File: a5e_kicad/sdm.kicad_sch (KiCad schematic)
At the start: 21 parts, among them U2 MX25U25645G, U7 A5EB013B-B23B

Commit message: Add LCSC part numbers and fix C102 footprint
Add a hidden LCSC field to 290 symbols from the JLCPCB parts match
(2026-10-23). Left without LCSC: U7, U15, L1 (not in the JLCPCB
library), C1/C2/C4 and L2-L5 (no value specified), J3 (no confident
match) and Y3 (the 12 pF Basic crystal does not suit the 27 pF load
caps). U2, U12, Y2 and J9 carry the exact-MPN LCSC numbers although
they currently show zero JLCPCB stock.

C102 (22U 6V3) had a 0201 footprint; no 22 uF 0201 part exists. Change
it to 0402 (C415703) like C5-C7.
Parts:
- D1, D2: LCSC (none) -> C3030991
- R10, R11, R12, R14, R15, R19, R20, R21, R8, R9: LCSC (none) -> C25744
- R16, R17: LCSC (none) -> C25130
- R18: LCSC (none) -> C4109
- R22: LCSC (none) -> C11702
- R4, R45, R7: LCSC (none) -> C25900
- U2: LCSC (none) -> C2802880
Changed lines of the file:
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@@
 			)
 		)
+		(property "LCSC" "C25744"
+			(at 80.772 93.98 90)
+			(hide yes)
+			(show_name no)
+			(do_not_autoplace no)
+			(effects
+				(font
+					(size 1.27 1.27)
+				)
+			)
+		)
 		(property "Datasheet" ""
 			(at 82.55 93.98 0)
@@
 			)
 		)
+		(property "LCSC" "C25744"
+			(at 219.202 26.67 90)
+			(hide yes)
+			(show_name no)
+			(do_not_autoplace no)
+			(effects
+				(font
+					(size 1.27 1.27)
+				)
+			)
+		)
 		(property "Datasheet" ""
 			(at 220.98 26.67 0)
@@
 			)
 		)
+		(property "LCSC" "C25744"
+			(at 70.612 93.98 90)
+			(hide yes)
+			(show_name no)
+			(do_not_autoplace no)
+			(effects
+				(font
+					(size 1.27 1.27)
+				)
+			)
+		)
 		(property "Datasheet" ""
 			(at 72.39 93.98 0)
@@
 			)
 		)
+		(property "LCSC" "C11702"
+			(at 229.362 26.67 90)
+			(hide yes)
+			(show_name no)
+			(do_not_autoplace no)
+			(effects
+				(font
+					(size 1.27 1.27)
+				)
+			)
+		)
 		(property "Datasheet" ""
 			(at 231.14 26.67 0)
@@
 			)
 		)
+		(property "LCSC" "C25744"
+			(at 75.692 93.98 90)
+			(hide yes)
+			(show_name no)
+			(do_not_autoplace no)
+			(effects
+				(font
+					(size 1.27 1.27)
+				)
+			)
+		)
 		(property "Datasheet" ""
 			(at 77.47 93.98 0)
@@
 			)
 		)
+		(property "LCSC" "C3030991"
+			(at 100.33 162.56 0)
+			(hide yes)
+			(show_name no)
+			(do_not_autoplace no)
+			(effects
+				(font
+					(size 1.27 1.27)
+				)
+			)
+		)
 		(property "Datasheet" "https://www.we-online.com/components/products/datasheet/150060RS75000.pdf"
 			(at 100.33 162.56 0)
@@
 			)
 		)
+		(property "LCSC" "C25744"
+			(at 87.122 46.99 90)
+			(hide yes)
+			(show_name no)
+			(do_not_autoplace no)
+			(effects
+				(font
+					(size 1.27 1.27)
+				)
+			)
+		)
 		(property "Datasheet" ""
 			(at 88.9 46.99 0)
@@
 			)
 		)
+		(property "LCSC" "C4109"
+			(at 188.722 123.19 90)
+			(hide yes)
+			(show_name no)
+			(do_not_autoplace no)
+			(effects
+				(font
+					(size 1.27 1.27)
+				)
+			)
+		)
 		(property "Datasheet" ""
 			(at 190.5 123.19 0)
@@
 			)
 		)
+		(property "LCSC" "C25744"
+			(at 214.122 26.67 90)
+			(hide yes)
+			(show_name no)
+			(do_not_autoplace no)
+			(effects
+				(font
+					(size 1.27 1.27)
+				)
+			)
+		)
 		(property "Datasheet" ""
 			(at 215.9 26.67 0)
@@
 			)
 		)
+		(property "LCSC" "C25130"
+			(at 110.49 164.338 90)
+			(hide yes)
+			(show_name no)
+			(do_not_autoplace no)
+			(effects
+				(font
+					(size 1.27 1.27)
+				)
+			)
+		)
 		(property "Datasheet" ""
 			(at 110.49 162.56 0)
@@
 			)
 		)
+		(property "LCSC" "C25744"
+			(at 82.042 46.99 90)
+			(hide yes)
+			(show_name no)
+			(do_not_autoplace no)
+			(effects
+				(font
+					(size 1.27 1.27)
+				)
+			)
+		)
 		(property "Datasheet" ""
 			(at 83.82 46.99 0)
@@
 			)
 		)
+		(property "LCSC" "C25900"
+			(at 60.452 93.98 90)
+			(hide yes)
+			(show_name no)
+			(do_not_autoplace no)
+			(effects
+				(font
+					(size 1.27 1.27)
+				)
+			)
+		)
 		(property "Datasheet" ""
 			(at 62.23 93.98 0)
@@
 			)
 		)
+		(property "LCSC" "C25130"
+			(at 110.49 182.118 90)
+			(hide yes)
+			(show_name no)
+			(do_not_autoplace no)
+			(effects
+				(font
+					(size 1.27 1.27)
+				)
+			)
+		)
 		(property "Datasheet" ""
 			(at 110.49 180.34 0)
@@
 			)
 		)
+		(property "LCSC" "C25900"
+			(at 55.372 133.35 90)
+			(hide yes)
+			(show_name no)
+			(do_not_autoplace no)
+			(effects
+				(font
+					(size 1.27 1.27)
+				)
+			)
+		)
 		(property "Datasheet" ""
 			(at 57.15 133.35 0)
@@
 			)
 		)
+		(property "LCSC" "C25900"
+			(at 50.292 133.35 90)
+			(hide yes)
+			(show_name no)
+			(do_not_autoplace no)
+			(effects
+				(font
+					(size 1.27 1.27)
+				)
+			)
+		)
 		(property "Datasheet" ""
 			(at 52.07 133.35 0)
@@
 			)
 		)
+		(property "LCSC" "C3030991"
+			(at 100.33 180.34 0)
+			(hide yes)
+			(show_name no)
+			(do_not_autoplace no)
+			(effects
+				(font
+					(size 1.27 1.27)
+				)
+			)
+		)
 		(property "Datasheet" "https://www.we-online.com/components/products/datasheet/150060RS75000.pdf"
 			(at 100.33 180.34 0)
@@
 			)
 		)
+		(property "LCSC" "C25744"
+			(at 224.282 26.67 90)
+			(hide yes)
+			(show_name no)
+			(do_not_autoplace no)
+			(effects
+				(font
+					(size 1.27 1.27)
+				)
+			)
+		)
 		(property "Datasheet" ""
 			(at 226.06 26.67 0)
@@
 			)
 		)
+		(property "LCSC" "C25744"
+			(at 92.202 46.99 90)
+			(hide yes)
+			(show_name no)
+			(do_not_autoplace no)
+			(effects
+				(font
+					(size 1.27 1.27)
+				)
+			)
+		)
 		(property "Datasheet" ""
 			(at 93.98 46.99 0)
@@
 			)
 		)
+		(property "LCSC" "C25744"
+			(at 65.532 93.98 90)
+			(hide yes)
+			(show_name no)
+			(do_not_autoplace no)
+			(effects
+				(font
+					(size 1.27 1.27)
+				)
+			)
+		)
 		(property "Datasheet" ""
 			(at 67.31 93.98 0)
@@
 			(at 46.99 55.88 0)
 			(hide yes)
+			(show_name no)
+			(do_not_autoplace no)
+			(effects
+				(font
+					(size 1.27 1.27)
+				)
+			)
+		)
+		(property "LCSC" "C2802880"
+			(at 46.99 55.88 0)
+			(hide yes)

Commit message: U12 -> H9HCNNN8KUMLHR-NME, U2 -> IS25WP128-RHLE (values, LCSC, datasheets)
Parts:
- U2: value MX25U25645G -> IS25WP128-RHLE; LCSC C2802880 -> C1349419
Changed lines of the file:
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@@
 			)
 		)
-		(property "Value" "MX25U25645G"
+		(property "Value" "IS25WP128-RHLE"
 			(at 46.99 70.88 0)
 			(show_name no)
@@
 			)
 		)
-		(property "LCSC" "C2802880"
+		(property "LCSC" "C1349419"
 			(at 46.99 55.88 0)
 			(hide yes)
@@
 			)
 		)
-		(property "Datasheet" "https://www.macronix.com/Lists/Datasheet/Attachments/8738/MX25U25645G,%201.8V,%20256Mb,%20v1.4.pdf"
+		(property "Datasheet" "https://www.lcsc.com/datasheet/C1349419.pdf"
 			(at 46.99 55.88 0)
 			(hide yes)
@@
 			)
 		)
-		(property "Description" "256Mb 1.8V QSPI NOR Flash, 24-ball CSP/BGA (5x5, A1 depopulated), SFDP + 1-1-1/1-4-4/4-4-4, dedicated RESET# - Agilex 5 SDM ASx4 boot compatible"
+		(property "Description" "128Mb 1.8V QSPI NOR flash, dedicated RESET# (A4), SFDP, 24-ball TFBGA 6x8 mm 5x5 array - Agilex 5 SDM ASx4 boot compatible"
 			(at 46.99 55.88 0)
 			(hide yes)

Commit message: Power/config review against the Altera docs: bank 6A, MSEL, resets, fabric clock
Checked against Pin Connection Guidelines 813266, Power Management UG
813161, Configuration UG 813773 and the data sheet 813918; findings are
in AGILEX_POWER_CONFIG_CHECKLIST.md.

- VCCIO_HVIO_6A moves from the VCCPT 1V8 regulator to 3V3. PCG table 32
  requires a dedicated VCCIO_HVIO supply. CE19 no longer takes the 1.8 V
  sdm_clk25.
- Y4 (YXC OT3225100MJBA4SL, 100 MHz 3.3 V CMOS, C4353707) drives the
  dangling clk100 net to AE11 (bank 6G PLLREFCLK1), giving the fabric a
  PLL reference that doesn't depend on the HPS. The clock sheet pin
  clk2_N is renamed clk100.
- MSEL 001 (AS fast) -> 011 (AS normal): fast mode needs all supplies
  ramped within 10 ms, which the sequenced regulators don't guarantee.
  R45 now goes to 1V8, and R4 gets its own GND.
- R264 10k pull-up on HPS_COLD_nRESET (SDM_IO10), as the PCG requires.
- R9/R10 (INIT_DONE/CONF_DONE pull-ups) DNP; the internal pull-downs
  hold the pins low until configuration.
- Note on the fpga_power sheet and the PCB (Cmts.User): ferrite + cap
  isolation filters on the PLL/ADC rails are recommended but not
  fitted yet.
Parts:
- added R264: 10K, Resistor_SMD:R_0402_1005Metric, symbol Device:R
- R10, R9: now not fitted
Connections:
- net 1V8: now also R45.2, R264.1
- net GND: no longer R45.2
- net ~{hpscold_rstn}: now also R264.2
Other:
- note added: "R264: HPS_COLD_nRESET pull-up, 1-10k to VCCIO_SDM (PCG 813266). MSEL = 011 (AS normal): R45 to 1V8. R9/R10 DNP: SDM_IO0/IO16 have internal pull-downs."
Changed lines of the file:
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@@
 	)
 	(junction
-		(at 57.15 139.7)
-		(diameter 0)
-		(color 0 0 0 0)
-	)
-	(junction
 		(at 74.93 87.63)
 		(diameter 0)
@@
 	(wire
 		(pts
-			(xy 57.15 139.7) (xy 52.07 139.7)
-		)
-		(stroke
-			(width 0)
-			(type default)
-		)
-	)
-	(wire
-		(pts
 			(xy 95.25 162.56) (xy 96.52 162.56)
 		)
@@
 		(on_board yes)
 		(in_pos_files yes)
-		(dnp no)
+		(dnp yes)
 		(property "Reference" "R9"
 			(at 72.39 90.17 0)
@@
 		(on_board yes)
 		(in_pos_files yes)
-		(dnp no)
+		(dnp yes)
 		(property "Reference" "R10"
 			(at 77.47 90.17 0)
@@
 	)
 	(symbol
-		(lib_id "power:GND")
-		(at 57.15 139.7 0)
+		(lib_id "power:+3V3")
+		(at 57.15 139.7 180)
 		(unit 1)
 		(body_style 1)
@@
 		(fields_autoplaced yes)
 		(property "Reference" "#PWR021"
-			(at 57.15 146.05 0)
+			(at 57.15 143.51 0)
 			(hide yes)
 			(show_name no)
@@
 			)
 		)
-		(property "Value" "GND"
-			(at 57.15 144.78 0)
+		(property "Value" "1V8"
+			(at 57.15 134.62 0)
 			(show_name no)
 			(do_not_autoplace no)
@@
 			)
 		)
-		(property "Description" "Power symbol creates a global label with name \"GND\" , ground"
+		(property "Description" "Power symbol creates a global label with name \"+3V3\""
 			(at 57.15 139.7 0)
 			(hide yes)
@@
 		)
 		(instances
-			(project "DBM_A5E013"
-				(path "/267d02d2-570f-41a1-8015-b378cedbc665/8aaf6c2b-ae6e-4499-806d-67948f95803c"
-					(reference "#PWR0202")
-					(unit 1)
-				)
-			)
 			(project "agilex_3_soc"
 				(path "/a5b98d95-6877-4284-904f-d04e32723ae0/8aaf6c2b-ae6e-4499-806d-67948f95803c"
@@
 		)
 	)
-)
+	(wire
+		(pts
+			(xy 82.55 87.63) (xy 87.63 87.63)
+		)
+		(stroke
+			(width 0)
+			(type default)
+		)
+	)
+	(junction
+		(at 82.55 87.63)
+		(diameter 0)
+		(color 0 0 0 0)
+	)
+	(wire
+		(pts
+			(xy 87.63 87.63) (xy 87.63 90.17)
+		)
+		(stroke
+			(width 0)
+			(type default)
+		)
+	)
+	(symbol
+		(lib_id "Device:R")
+		(at 87.63 93.98 0)
+		(unit 1)
+		(body_style 1)
+		(exclude_from_sim no)
+		(in_bom yes)
+		(on_board yes)
+		(in_pos_files yes)
+		(dnp no)
+		(property "Reference" "R264"
+			(at 87.63 90.17 0)
+			(show_name no)
+			(do_not_autoplace no)
+			(effects
+				(font
+					(size 1.27 1.27)
+				)
+				(justify left)
+			)
+		)
+		(property "Value" "10K"
+			(at 87.63 97.79 0)
+			(show_name no)
+			(do_not_autoplace no)
+			(effects
+				(font
+					(size 1.27 1.27)
+				)
+				(justify left)
+			)
+		)
+		(property "Footprint" "Resistor_SMD:R_0402_1005Metric"
+			(at 85.852 93.98 90)
+			(hide yes)
+			(show_name no)
+			(do_not_autoplace no)
+			(effects
+				(font
+					(size 1.27 1.27)
+				)
+			)
+		)
+		(property "LCSC" "C25744"
+			(at 85.852 93.98 90)
+			(hide yes)
+			(show_name no)
+			(do_not_autoplace no)
+			(effects
+				(font
+					(size 1.27 1.27)
+				)
+			)
+		)
+		(property "Datasheet" ""
+			(at 87.63 93.98 0)
+			(hide yes)
+			(show_name no)
+			(do_not_autoplace no)
+			(effects
+				(font
+					(size 1.27 1.27)
+				)
+			)
+		)
+		(property "Description" "Resistor"
+			(at 87.63 93.98 0)
+			(hide yes)
+			(show_name no)
+			(do_not_autoplace no)
+			(effects
+				(font
+					(size 1.27 1.27)
+				)
+			)
+		)
+		(pin "2"
+		)
+		(pin "1"
+		)
+		(instances
+			(project "agilex_3_soc"
+				(path "/a5b98d95-6877-4284-904f-d04e32723ae0/8aaf6c2b-ae6e-4499-806d-67948f95803c"
+					(reference "R264")
+					(unit 1)
+				)
+			)
+		)
+	)	(wire
+		(pts
+			(xy 87.63 97.79) (xy 87.63 104.14)
+		)
+		(stroke
+			(width 0)
+			(type default)
+		)
+	)
+	(label "~{hps_cold_rstn}"
+		(at 87.63 104.14 0)
+		(effects
+			(font
+				(size 1.27 1.27)
+			)
+			(justify left bottom)
+		)
+	)
+	(text "R264: HPS_COLD_nRESET pull-up, 1-10k to VCCIO_SDM (PCG 813266).\nMSEL = 011 (AS normal): R45 to 1V8. R9/R10 DNP: SDM_IO0/IO16 have internal pull-downs."
+		(exclude_from_sim no)
+		(at 52.07 147.32 0)
+		(effects
+			(font
+				(size 1.27 1.27)
+			)
+			(justify left)
+		)
+	)
+	(symbol
+		(lib_id "power:GND")
+		(at 52.07 139.7 0)
+		(unit 1)
+		(body_style 1)
+		(exclude_from_sim no)
+		(in_bom yes)
+		(on_board yes)
+		(in_pos_files yes)
+		(dnp no)
+		(fields_autoplaced yes)
+		(property "Reference" "#PWR1562"
+			(at 52.07 133.35 0)
+			(hide yes)
+			(show_name no)
+			(do_not_autoplace no)
+			(effects
+				(font
+					(size 1.27 1.27)
+				)
+			)
+		)
+		(property "Value" "GND"
+			(at 52.07 134.62 0)
+			(show_name no)
+			(do_not_autoplace no)
+			(effects
+				(font
+					(size 1.27 1.27)
+				)
+			)
+		)
+		(property "Footprint" ""
+			(at 52.07 139.7 0)
+			(hide yes)
+			(show_name no)
+			(do_not_autoplace no)
+			(effects
+				(font
+					(size 1.27 1.27)
+				)
+			)
+		)
+		(property "Datasheet" ""
+			(at 52.07 139.7 0)
+			(hide yes)
+			(show_name no)
+			(do_not_autoplace no)
+			(effects
+				(font
+					(size 1.27 1.27)
+				)
+			)
+		)
+		(property "Description" "Power symbol creates a global label with name \"GND\" , ground"
+			(at 52.07 139.7 0)
+			(hide yes)
+			(show_name no)
+			(do_not_autoplace no)
+			(effects
+				(font
+					(size 1.27 1.27)
+				)
+			)
+		)
+		(pin "1"
+		)
+		(instances
+			(project "agilex_3_soc"
+				(path "/a5b98d95-6877-4284-904f-d04e32723ae0/8aaf6c2b-ae6e-4499-806d-67948f95803c"
+					(reference "#PWR1562")
+					(unit 1)
+				)
+			)
+		)
+	))

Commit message: Schematic reorg step 1: remove dangling stubs and stale notes, correct notes, fill title blocks
Netlist: 0 renamed, 0 connectivity diffs; DRC parity 0. ERC 315 -> 242.
Plan refreshed for the eMMC, RTL8211FDI, TPS548A28 and the tuned LPDDR4 (IOBANK 3 sheet name kept).
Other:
- title: (none) -> SDM: configuration, QSPI boot flash, status LEDs
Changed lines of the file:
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@@
 	(paper "A4")
 	(title_block
-		(rev "0.1")
+		(title "SDM: configuration, QSPI boot flash, status LEDs")
+		(rev "${REVISION}")
+		(comment 1 "${BOARD}")
 	)
 	(text "msel0"
@@
 	)
 	(bus_entry
-		(at 104.14 58.42)
-		(size -2.54 2.54)
-		(stroke
-			(width 0)
-			(type default)
-		)
-	)
-	(bus_entry
 		(at 187.96 35.56)
 		(size 2.54 2.54)
@@
 		(at 180.34 91.44)
 		(size 2.54 2.54)
-		(stroke
-			(width 0)
-			(type default)
-		)
-	)
-	(bus_entry
-		(at 104.14 60.96)
-		(size -2.54 2.54)
 		(stroke
 			(width 0)
@@
 		(stroke
 			(width 0)
-			(type default)
-		)
-	)
-	(bus_entry
-		(at 104.14 53.34)
-		(size -2.54 2.54)
-		(stroke
-			(width 0)
-			(type default)
-		)
-	)
-	(bus_entry
-		(at 104.14 55.88)
-		(size -2.54 2.54)
-		(stroke
-			(width 0)

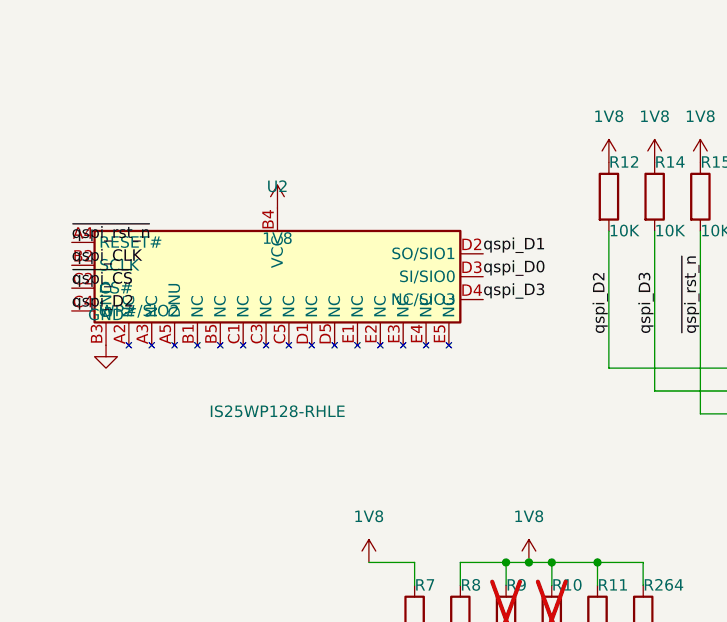
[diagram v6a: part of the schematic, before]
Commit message: Schematic reorg step 3: U42 cluster on grid, U2 symbol redrawn, notes wrapped inside the frame
Netlist: 0 renamed, 0 connectivity diffs; DRC parity 0. ERC 223 -> 199 (no off-grid endpoints).
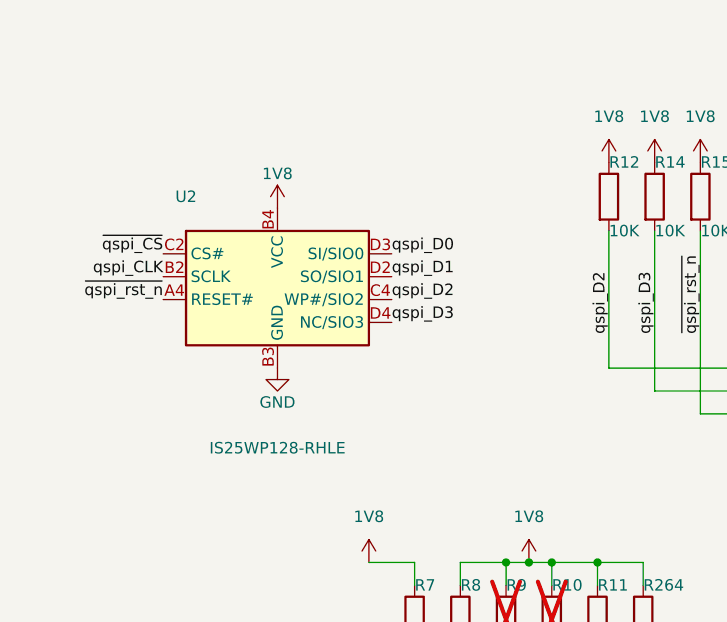
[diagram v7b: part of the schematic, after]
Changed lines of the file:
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@@
 	)
 	(label "qspi_D1"
-		(at 69.85 53.34 0)
+		(at 59.69 55.88 0)
 		(effects
 			(font
@@
 	)
 	(label "~{qspi_CS}"
-		(at 24.13 57.15 0)
+		(at 34.29 53.34 180)
 		(effects
 			(font
 				(size 1.27 1.27)
 			)
-			(justify left bottom)
+			(justify right bottom)
 		)
 	)
@@
 	)
 	(label "qspi_D2"
-		(at 24.13 59.69 0)
+		(at 59.69 58.42 0)
 		(effects
 			(font
@@
 	)
 	(label "~{qspi_rst_n}"
-		(at 24.13 52.07 0)
+		(at 34.29 58.42 180)
 		(effects
 			(font
 				(size 1.27 1.27)
 			)
-			(justify left bottom)
+			(justify right bottom)
 		)
 	)
@@
 	)
 	(label "qspi_D0"
-		(at 69.85 55.88 0)
+		(at 59.69 53.34 0)
 		(effects
 			(font
@@
 	)
 	(label "qspi_D3"
-		(at 69.85 58.42 0)
+		(at 59.69 60.96 0)
 		(effects
 			(font
@@
 	)
 	(label "qspi_CLK"
-		(at 24.13 54.61 0)
+		(at 34.29 55.88 180)
 		(effects
 			(font
 				(size 1.27 1.27)
 			)
-			(justify left bottom)
+			(justify right bottom)
 		)
 	)
@@
 		)
 		(property "Value" "1V8"
-			(at 46.99 51.64 0)
+			(at 46.99 44.45 0)
 			(show_name no)
 			(do_not_autoplace no)
@@
 	(symbol
 		(lib_id "power:GND")
-		(at 27.94 63.5 0)
+		(at 46.99 66.04 0)
 		(unit 1)
 		(body_style 1)
@@
 		(dnp no)
 		(property "Reference" "#PWR023"
-			(at 30.99 63.5 0)
+			(at 50.04 66.04 0)
 			(hide yes)
 			(show_name no)
@@
 		)
 		(property "Value" "GND"
-			(at 27.94 60.12 0)
+			(at 46.99 69.85 0)
 			(show_name no)
 			(do_not_autoplace no)
@@
 		)
 		(property "Footprint" ""
-			(at 27.94 63.5 0)
+			(at 46.99 66.04 0)
 			(hide yes)
 			(show_name no)
@@
 		)
 		(property "Datasheet" ""
-			(at 27.94 63.5 0)
+			(at 46.99 66.04 0)
 			(hide yes)
 			(show_name no)
@@
 		(fields_autoplaced yes)
 		(property "Reference" "U2"
-			(at 46.99 45.88 0)
+			(at 36.83 46.99 0)
 			(show_name no)
 			(do_not_autoplace no)
@@
 		)
 		(property "Value" "IS25WP128-RHLE"
-			(at 46.99 70.88 0)
+			(at 46.99 74.93 0)
 			(show_name no)
 			(do_not_autoplace no)
